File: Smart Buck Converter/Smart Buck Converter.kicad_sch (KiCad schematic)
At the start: 8 parts, among them U2 ATSAMD21E18A-A, X1 830003000

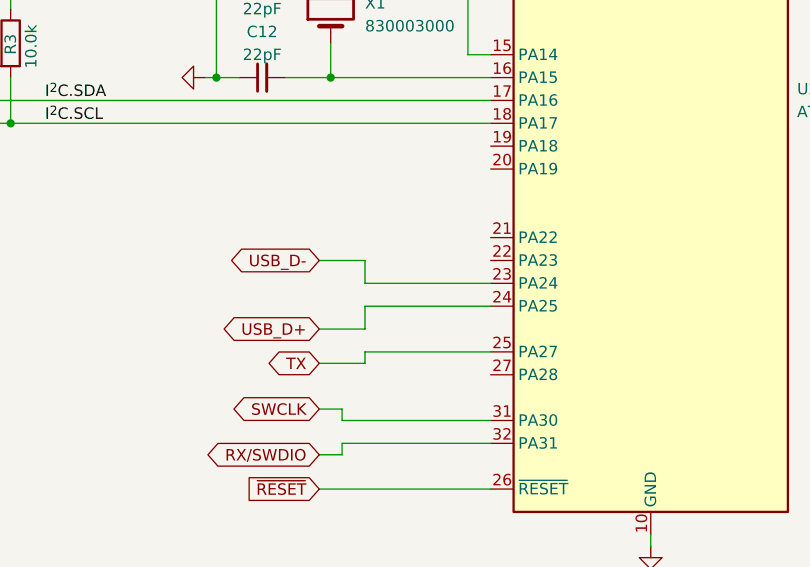
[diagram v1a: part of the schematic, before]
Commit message: Revision 2 update
Regenerated gerber files to rev 2 design, made minor changes to PCB layout before exporting. Changed I2C interface connector from 4-pin right angle style to vertical style, added the new connector the the KiCad footprints library.
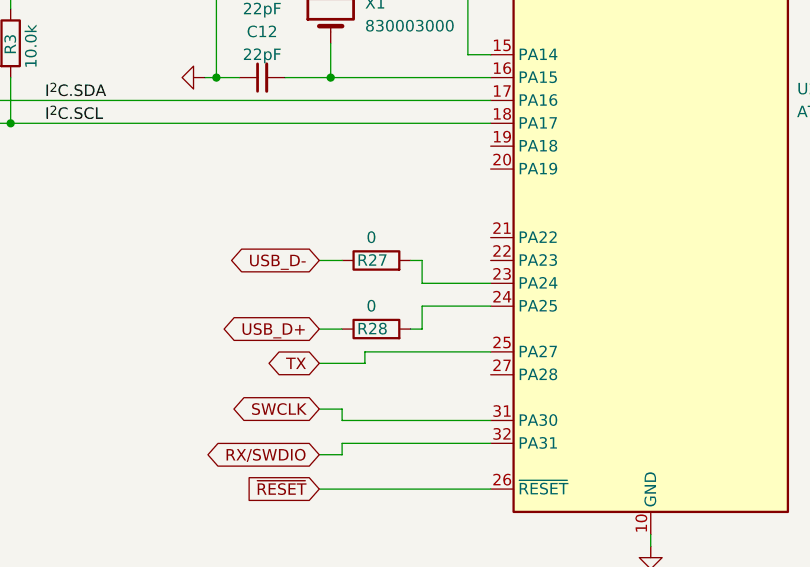
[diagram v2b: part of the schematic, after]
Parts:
- added R27, R28: 0, Resistor_SMD:R_0805_2012Metric, symbol Device:R
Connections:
- net USB_D+: now also R28.1; no longer U2.24 (PA25)
- net USB_D-: now also R27.1; no longer U2.23 (PA24)
- new net: R27.2, U2.23 (PA24)
- new net: R28.2, U2.24 (PA25)
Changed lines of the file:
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@@
+    (stroke (width 0) (type default))
+  )
+  (wire (pts (xy 199.39 111.76) (xy 207.01 111.76))
     (stroke (width 0) (type default))
   )
@@
     (stroke (width 0) (type default))
   )
-  (wire (pts (xy 193.04 111.76) (xy 193.04 109.22))
+  (wire (pts (xy 198.12 109.22) (xy 199.39 109.22))
     (stroke (width 0) (type default))
   )
@@
     (stroke (width 0) (type default))
   )
+  (wire (pts (xy 199.39 116.84) (xy 199.39 114.3))
+    (stroke (width 0) (type default))
+  )
   (wire (pts (xy 153.67 88.9) (xy 153.67 93.98))
     (stroke (width 0) (type default))
@@
     (stroke (width 0) (type default))
   )
-  (wire (pts (xy 187.96 116.84) (xy 193.04 116.84))
-    (stroke (width 0) (type default))
-  )
   (wire (pts (xy 190.5 129.54) (xy 207.01 129.54))
     (stroke (width 0) (type default))
@@
     (stroke (width 0) (type default))
   )
+  (wire (pts (xy 187.96 109.22) (xy 190.5 109.22))
+    (stroke (width 0) (type default))
+  )
   (wire (pts (xy 189.23 85.09) (xy 189.23 88.9))
     (stroke (width 0) (type default))
@@
     (stroke (width 0) (type default))
   )
-  (wire (pts (xy 193.04 109.22) (xy 187.96 109.22))
-    (stroke (width 0) (type default))
-  )
   (wire (pts (xy 148.59 91.44) (xy 207.01 91.44))
     (stroke (width 0) (type default))
@@
     (stroke (width 0) (type default))
   )
+  (wire (pts (xy 199.39 114.3) (xy 207.01 114.3))
+    (stroke (width 0) (type default))
+  )
   (wire (pts (xy 153.67 81.28) (xy 153.67 80.01))
     (stroke (width 0) (type default))
   )
+  (wire (pts (xy 187.96 116.84) (xy 190.5 116.84))
+    (stroke (width 0) (type default))
+  )
+  (wire (pts (xy 199.39 109.22) (xy 199.39 111.76))
+    (stroke (width 0) (type default))
+  )
   (wire (pts (xy 224.79 139.7) (xy 224.79 140.97))
     (stroke (width 0) (type default))
   )
-  (wire (pts (xy 193.04 114.3) (xy 207.01 114.3))
-    (stroke (width 0) (type default))
-  )
   (bus (pts (xy 139.7 86.36) (xy 142.24 86.36))
     (stroke (width 0) (type default))
@@
     (stroke (width 0) (type default))
   )
+  (wire (pts (xy 198.12 116.84) (xy 199.39 116.84))
+    (stroke (width 0) (type default))
+  )
   (wire (pts (xy 151.13 71.12) (xy 151.13 80.01))
     (stroke (width 0) (type default))
   )
-  (wire (pts (xy 193.04 116.84) (xy 193.04 114.3))
-    (stroke (width 0) (type default))
-  )
   (wire (pts (xy 41.91 71.12) (xy 44.45 71.12))
     (stroke (width 0) (type default))
@@
   )
   (wire (pts (xy 38.1 38.1) (xy 40.64 38.1))
-    (stroke (width 0) (type default))
-  )
-  (wire (pts (xy 207.01 111.76) (xy 193.04 111.76))
     (stroke (width 0) (type default))
   )
@@
         )
       )
+    )
+  )
+  (symbol (lib_id "Device:R") (at 194.31 109.22 90) (unit 1)
+    (in_bom yes) (on_board yes) (dnp no)
+    (property "Reference" "R27" (at 195.58 109.22 90)
+      (effects (font (size 1.27 1.27)) (justify left))
+    )
+    (property "Value" "0" (at 194.31 106.68 90)
+      (effects (font (size 1.27 1.27)) (justify left))
+    )
+    (property "Footprint" "Resistor_SMD:R_0805_2012Metric" (at 194.31 110.998 90)
+      (effects (font (size 1.27 1.27)) hide)
+    )
+    (property "Datasheet" "~" (at 194.31 109.22 0)
+      (effects (font (size 1.27 1.27)) hide)
+    )
+    (pin "1")
+    (pin "2")
+    (instances
+      (project "Smart Buck Converter"
+        (path "/e63e39d7-6ac0-4ffd-8aa3-1841a4541b55"
+          (reference "R27") (unit 1)
+        )
+      )
+    )
+  )
+  (symbol (lib_id "Device:R") (at 194.31 116.84 90) (unit 1)
+    (in_bom yes) (on_board yes) (dnp no)
+    (property "Reference" "R28" (at 195.58 116.84 90)
+      (effects (font (size 1.27 1.27)) (justify left))
+    )
+    (property "Value" "0" (at 194.31 114.3 90)
+      (effects (font (size 1.27 1.27)) (justify left))
+    )
+    (property "Footprint" "Resistor_SMD:R_0805_2012Metric" (at 194.31 118.618 90)
+      (effects (font (size 1.27 1.27)) hide)
+    )
+    (property "Datasheet" "~" (at 194.31 116.84 0)
+      (effects (font (size 1.27 1.27)) hide)
+    )
+    (pin "1")
+    (pin "2")
+    (instances
+      (project "Smart Buck Converter"
+        (path "/e63e39d7-6ac0-4ffd-8aa3-1841a4541b55"
+          (reference "R28") (unit 1)
+        )
+      )
